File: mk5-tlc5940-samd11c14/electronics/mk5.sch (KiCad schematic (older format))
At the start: 49 parts, among them J1 Conn_01x08_Male, J10 Conn_01x01, J11 Conn_01x01, J12 Conn_01x01, J13 Conn_01x01, J14 Conn_01x01, J15 Conn_01x01, J16 Conn_01x01, J17 Conn_01x01, J18 Conn_01x01, J19 Conn_01x01, J2 USB, J20 Conn_01x01, J21 Conn_01x01, J22 Conn_01x01, J23 +LED, J24 +LED, J25 +LED, J26 +LED, J27 +LED, J3 OUT15, J4 GS2, J6 +LED, J7 Conn_01x01, J8 Conn_01x01, J9 Conn_01x01, Q1 MOSFET 20V 3A, SW1 BTN, U1 USBLC6-2SC6, U2 MCP1702-3302_SOT23, U3 SAMD11C14A, U4 TLC5940PWP

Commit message: Start refactoring for QFN24 version
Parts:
- removed J1: Conn_01x08_Male, SMD-pads:CONN_8_SMD_FLAT, symbol Conn_01x08_Male
- removed R3, R4: 680, Resistors_SMD:R_0603, symbol R
- removed U3: SAMD11C14A, Housings_SOIC:SOIC-14_3.9x8.7mm_Pitch1.27mm, symbol SAMD11C14A
- added J1: Conn_01x06_Male, SMD-pads:CONN_6_SMD_FLAT, symbol Conn_01x06_Male
- added U3: SAMD11D14A-M, Housings_DFN_QFN:QFN-24_4x4mm_Pitch0.5mm, symbol SAMD11D14A-M
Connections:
- net labels added: BLANK, BUTTON, Button, RESET, SCLK, SIN, SWCLK, SWDIO
- net labels removed: BLANK/RESET, SCK/SWCLK, SIN/SWDIO
- wire segments 133 -> 118
- no-connect marks 3 -> 11
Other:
- note added: "Do not use PA10, PA11, PA17, PA27 \nfor compatibility with SOIC-20"
- moved on the sheet: C3, C4, D3, J10, J11, J12, J13, J14, J15, J16, J17, J18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

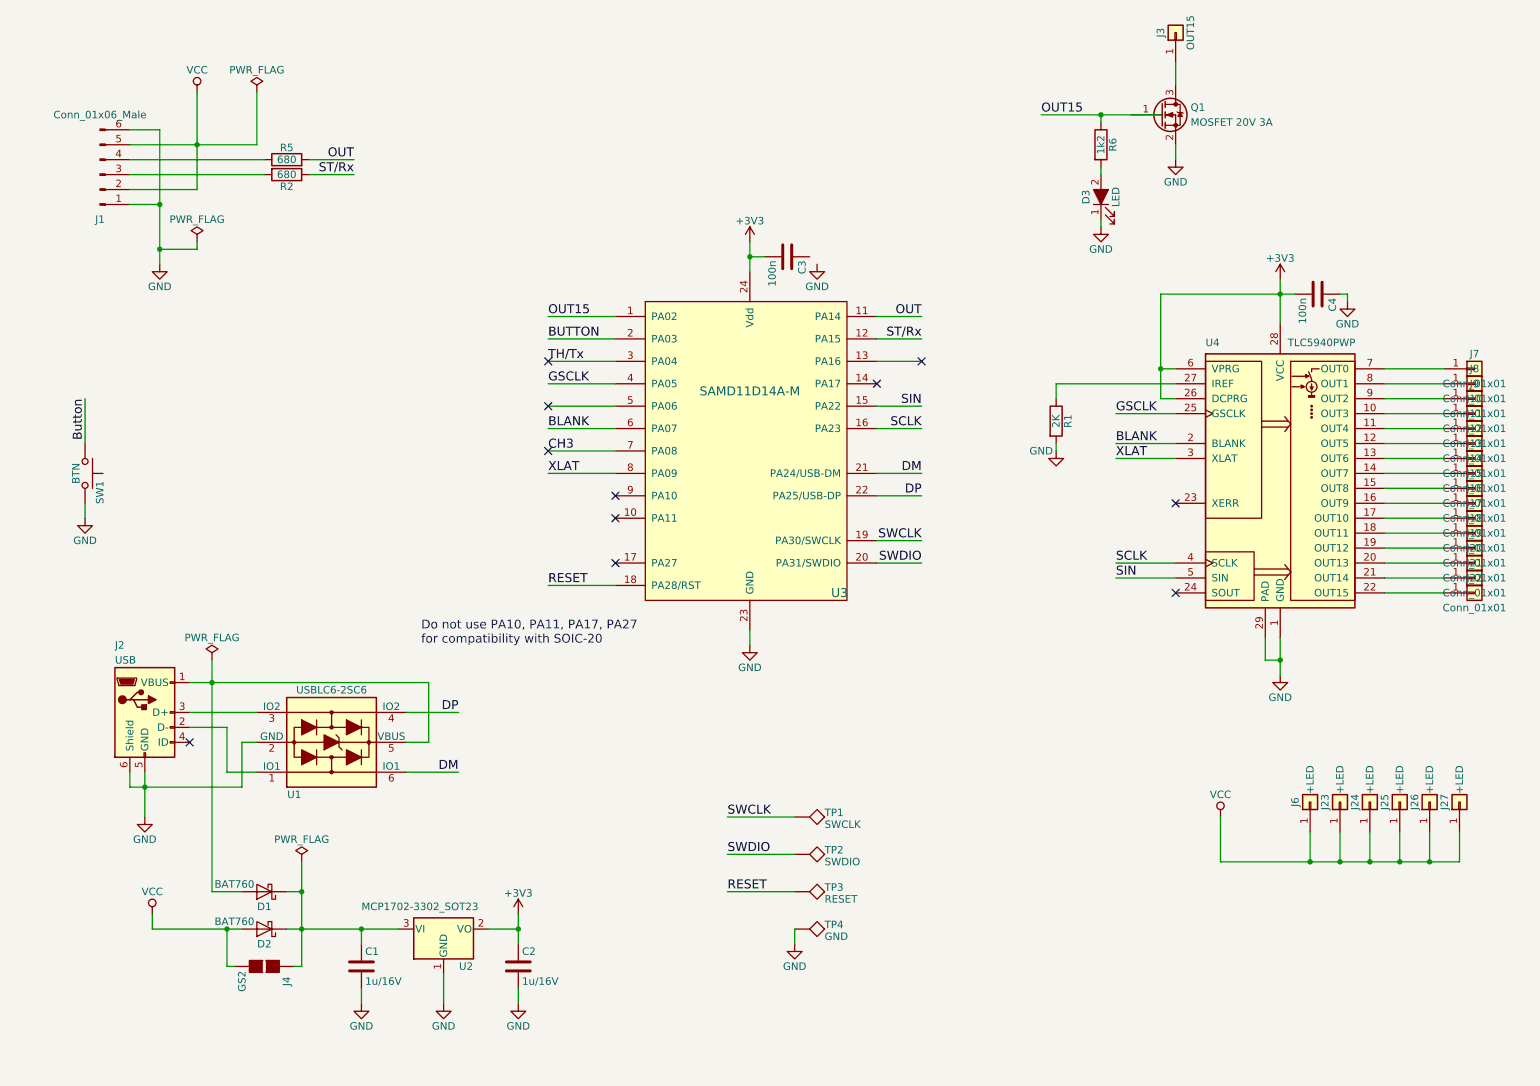
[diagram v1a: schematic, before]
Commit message: Try to figure out component placement for QFN version
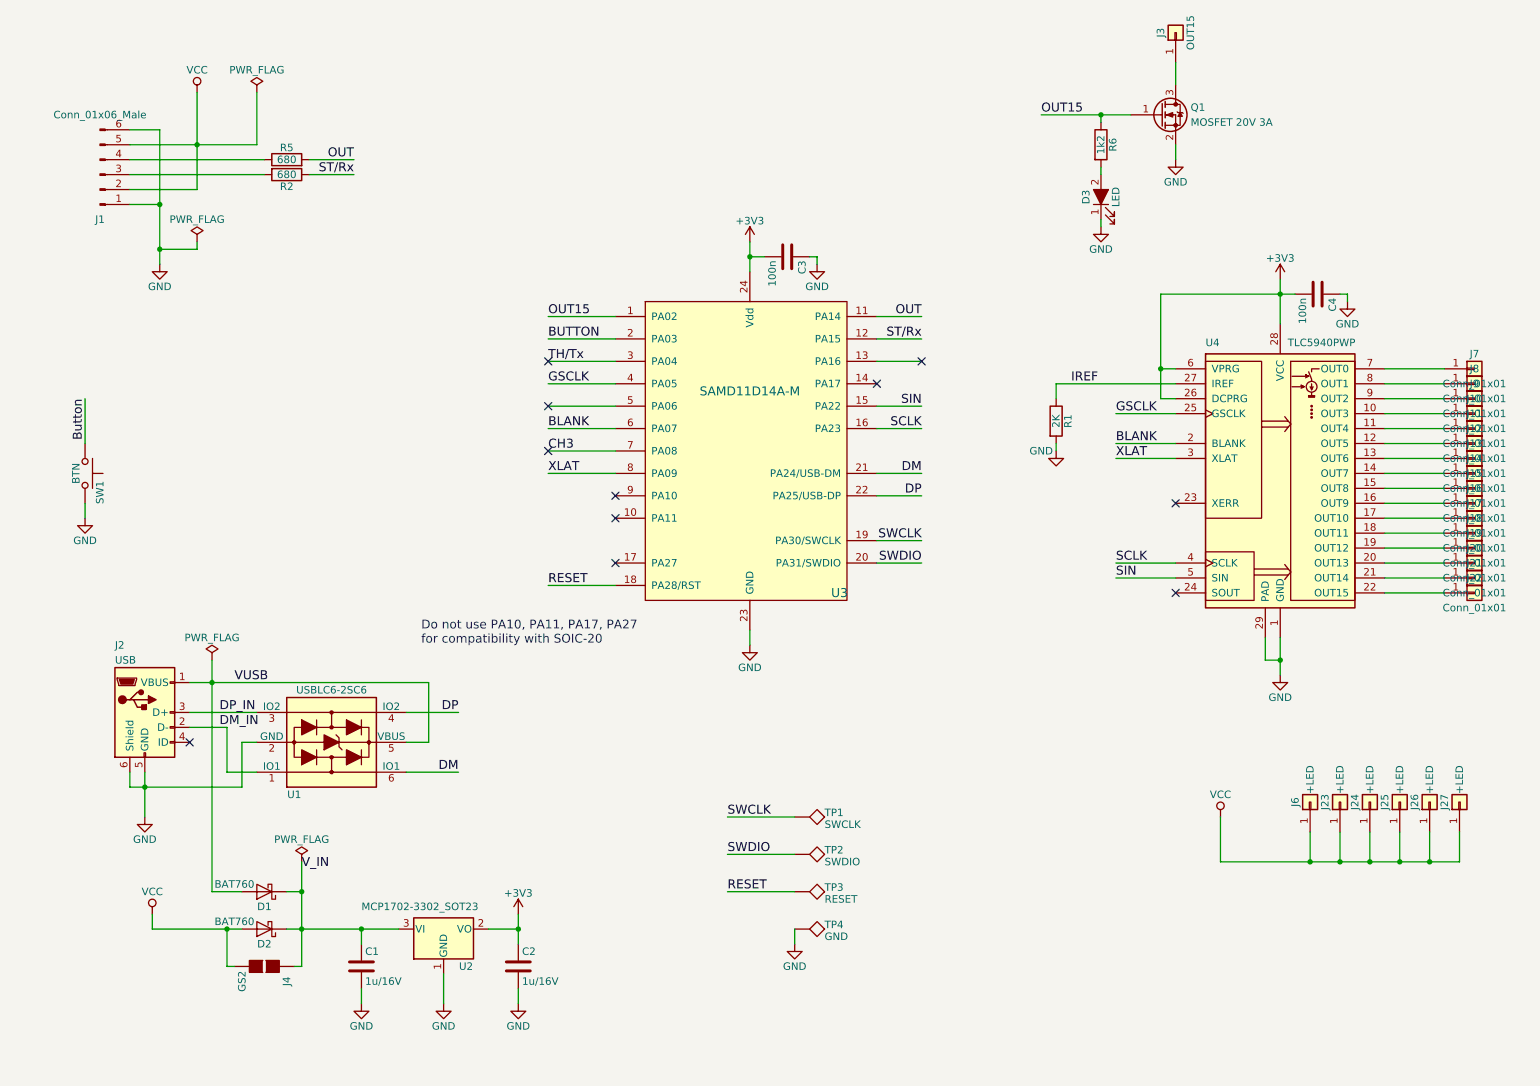
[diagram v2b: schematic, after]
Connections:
- net GND: now also C3.1
- net OUT15: now also Q1.1 (G)
- net IREF: now reaches R1.1, U4.27 (IREF)
- net VUSB: now reaches D1.2 (A), J2.1 (VBUS), U1.5 (VBUS)
- net DM_IN: now reaches J2.2 (D-), U1.1 (IO1)
- net DP_IN: now reaches J2.3 (D+), U1.3 (IO2)
- net V_IN: now reaches C1.1, D1.1 (K), D2.1 (K), J4.1 (G1), U2.3 (VI)
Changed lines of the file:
@@
 	4350 2600 4800 2600
 Wire Wire Line
-	7650 1250 8450 1250
+	7650 1250 8250 1250
 $Comp
 L R R2
@@
 Text Notes 3500 4800 0    59   ~ 0
 Do not use PA10, PA11, PA17, PA27 \nfor compatibility with SOIC-20
+Wire Wire Line
+	6100 2200 6150 2200
+Wire Wire Line
+	6150 2200 6150 2250
+Text Label 2250 5050 0    60   ~ 0
+VUSB
+Text Label 2150 5250 0    60   ~ 0
+DP_IN
+Text Label 2150 5350 0    60   ~ 0
+DM_IN
+Text Label 2700 6300 0    60   ~ 0
+V_IN
+Text Label 7850 3050 0    60   ~ 0
+IREF
 $EndSCHEMATC

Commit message: Change MCU pins for better layout
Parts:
- removed D1, D2: BAT760, Diodes_SMD:D_SOD-323_HandSoldering, symbol D_Schottky
- added D1: BAT54C, TO_SOT_Packages_SMD:SOT-23, symbol BAT54C
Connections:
- net BLANK: now also U3.7 (PA08); no longer U3.6 (PA07)
- net CH3: now also U3.16 (PA23); no longer U3.7 (PA08)
- net GSCLK: now also U3.13 (PA16); no longer U3.4 (PA05)
- net SCLK: now also U3.4 (PA05); no longer U3.16 (PA23)
- net SIN: now also U3.3 (PA04); no longer U3.15 (PA22)
- net TH/Tx: now also U3.15 (PA22); no longer U3.3 (PA04)
- net VCC: now also J4.1 (G1), D1.1; no longer J4.2 (G2)
- net VUSB: now also D1.2
- net V_IN: now also J4.2 (G2), D1.3; no longer J4.1 (G1)
- net XLAT: now also U3.6 (PA07); no longer U3.8 (PA09)
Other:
- moved on the sheet: J4
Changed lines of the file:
@@
 EESchema Schematic File Version 2
 LIBS:SAM_D11
+LIBS:bat54c
 LIBS:power
 LIBS:device
@@
 	1    0    0    -1
 $EndComp
-$Comp
-L D_Schottky D2
-U 1 1 59C47D22
-P 2450 6700
-F 0 "D2" H 2450 6800 50  0000 C CNN
-F 1 "BAT760" H 2650 6650 50  0000 C CNN
-F 2 "Diodes_SMD:D_SOD-323_HandSoldering" H 2450 6700 50  0001 C CNN
-F 3 "" H 2450 6700 50  0001 C CNN
-	1    2450 6700
-	-1   0    0    1
-$EndComp
-$Comp
-L D_Schottky D1
-U 1 1 59C47DAA
-P 2450 6450
-F 0 "D1" H 2450 6550 50  0000 C CNN
-F 1 "BAT760" H 2650 6400 50  0000 C CNN
-F 2 "Diodes_SMD:D_SOD-323_HandSoldering" H 2450 6450 50  0001 C CNN
-F 3 "" H 2450 6450 50  0001 C CNN
-	1    2450 6450
-	-1   0    0    1
-$EndComp
 Wire Wire Line
 	5700 4700 5700 4800
@@
 	3650 7000 3650 7200
 Wire Wire Line
-	2600 6700 3350 6700
-Wire Wire Line
 	3100 6700 3100 6800
 Wire Wire Line
@@
 	3100 7100 3100 7200
 Connection ~ 3100 6700
-Wire Wire Line
-	2600 6450 2700 6450
-Wire Wire Line
-	2700 6250 2700 6950
 Connection ~ 2700 6700
 Wire Wire Line
-	2100 4900 2100 6450
-Wire Wire Line
-	2100 6450 2300 6450
-Wire Wire Line
-	1700 6700 2300 6700
+	2100 4900 2100 6400
 $Comp
 L Conn_01x01 J3
@@
 L PWR_FLAG #FLG016
 U 1 1 59C4CC7B
-P 2700 6250
-F 0 "#FLG016" H 2700 6325 50  0001 C CNN
-F 1 "PWR_FLAG" H 2700 6400 50  0000 C CNN
-F 2 "" H 2700 6250 50  0001 C CNN
-F 3 "" H 2700 6250 50  0001 C CNN
-	1    2700 6250
-	1    0    0    -1
-$EndComp
-Connection ~ 2700 6450
+P 2700 6550
+F 0 "#FLG016" H 2700 6625 50  0001 C CNN
+F 1 "PWR_FLAG" H 2700 6700 50  0000 C CNN
+F 2 "" H 2700 6550 50  0001 C CNN
+F 3 "" H 2700 6550 50  0001 C CNN
+	1    2700 6550
+	1    0    0    -1
+$EndComp
 $Comp
 L GND #PWR017
@@
 L VCC #PWR019
 U 1 1 59C4E307
-P 1700 6600
-F 0 "#PWR019" H 1700 6450 50  0001 C CNN
-F 1 "VCC" H 1700 6750 50  0000 C CNN
-F 2 "" H 1700 6600 50  0001 C CNN
-F 3 "" H 1700 6600 50  0001 C CNN
-	1    1700 6600
-	1    0    0    -1
-$EndComp
-Wire Wire Line
-	1700 6600 1700 6700
+P 1700 6950
+F 0 "#PWR019" H 1700 6800 50  0001 C CNN
+F 1 "VCC" H 1700 7100 50  0000 C CNN
+F 2 "" H 1700 6950 50  0001 C CNN
+F 3 "" H 1700 6950 50  0001 C CNN
+	1    1700 6950
+	1    0    0    -1
+$EndComp
+Wire Wire Line
+	1700 6950 1700 7100
 Wire Wire Line
 	2000 1100 2000 1750
-Wire Wire Line
-	4350 2600 4800 2600
 Wire Wire Line
 	7650 1250 8250 1250
@@
 	2000 2150 1750 2150
 Connection ~ 1750 2150
-Text Label 4350 3650 0    60   ~ 0
+Text Label 4350 3350 0    60   ~ 0
 XLAT
 Text Label 4350 2600 0    60   ~ 0
@@
 L GS2 J4
 U 1 1 59DCA798
-P 2450 6950
-F 0 "J4" H 2550 7100 50  0000 C CNN
-F 1 "GS2" H 2550 6801 50  0000 C CNN
-F 2 "SMD-pads:SMD_solder_jumper_2pin" V 2524 6950 50  0001 C CNN
-F 3 "" H 2450 6950 50  0001 C CNN
-	1    2450 6950
-	0    1    1    0
-$EndComp
-Wire Wire Line
-	2700 6950 2650 6950
-Wire Wire Line
-	2250 6950 2200 6950
-Wire Wire Line
-	2200 6950 2200 6700
-Connection ~ 2200 6700
+P 2500 6900
+F 0 "J4" H 2600 7050 50  0000 C CNN
+F 1 "GS2" H 2600 6751 50  0000 C CNN
+F 2 "SMD-pads:SMD_solder_jumper_2pin" V 2574 6900 50  0001 C CNN
+F 3 "" H 2500 6900 50  0001 C CNN
+	1    2500 6900
+	-1   0    0    1
+$EndComp
 Wire Wire Line
 	9250 4750 9250 5000
@@
 NoConn ~ 6550 3050
 NoConn ~ 4800 4250
-Text Label 4350 3350 0    60   ~ 0
+Text Label 4350 3500 0    60   ~ 0
 BLANK
 Wire Wire Line
 	4800 2900 4350 2900
-Text Label 4350 2900 0    60   ~ 0
+Text Label 6850 3200 2    60   ~ 0
 TH/Tx
-Text Label 4350 3050 0    60   ~ 0
+Text Label 6850 2900 2    60   ~ 0
 GSCLK
 Wire Wire Line
@@
 Wire Wire Line
 	4800 3500 4350 3500
-Text Label 4350 3500 0    60   ~ 0
+Text Label 6850 3350 2    60   ~ 0
 CH3
 $Comp
@@
 	1    0    0    1
 $EndComp
-NoConn ~ 4350 3500
-NoConn ~ 4350 2900
 Wire Wire Line
 	6550 3350 6850 3350
-Text Label 6850 3350 2    60   ~ 0
+Text Label 4350 3050 0    60   ~ 0
 SCLK
-Text Label 6850 3200 2    60   ~ 0
+Text Label 4350 2900 0    60   ~ 0
 SIN
 Wire Wire Line
@@
 Wire Wire Line
 	6550 2900 6850 2900
-NoConn ~ 6850 2900
 Wire Wire Line
 	4800 3200 4350 3200
-NoConn ~ 4350 3200
 Text Notes 3500 4800 0    59   ~ 0
 Do not use PA10, PA11, PA17, PA27 \nfor compatibility with SOIC-20
@@
 Text Label 2150 5350 0    60   ~ 0
 DM_IN
-Text Label 2700 6300 0    60   ~ 0
+Text Label 2800 6700 0    60   ~ 0
 V_IN
 Text Label 7850 3050 0    60   ~ 0
 IREF
+Wire Wire Line
+	4800 2600 4350 2600
+NoConn ~ 6850 3200
+NoConn ~ 6850 3350
+NoConn ~ 4350 3200
+NoConn ~ 4350 3650
+$Comp
+L BAT54C D1
+U 1 1 5A105797
+P 2100 6700
+F 0 "D1" H 2125 6550 50  0000 L CNN
+F 1 "BAT54C" H 1850 6825 50  0000 L CNN
+F 2 "TO_SOT_Packages_SMD:SOT-23" H 2175 6825 50  0001 L CNN
+F 3 "" H 1970 6700 50  0001 C CNN
+	1    2100 6700
+	0    -1   -1   0
+$EndComp
+Wire Wire Line
+	1700 7100 2500 7100
+Wire Wire Line
+	2100 7100 2100 7000
+Connection ~ 2100 7100
+Wire Wire Line
+	2300 6700 3350 6700
+Connection ~ 2500 6700
+Wire Wire Line
+	2700 6550 2700 6700
 $EndSCHEMATC

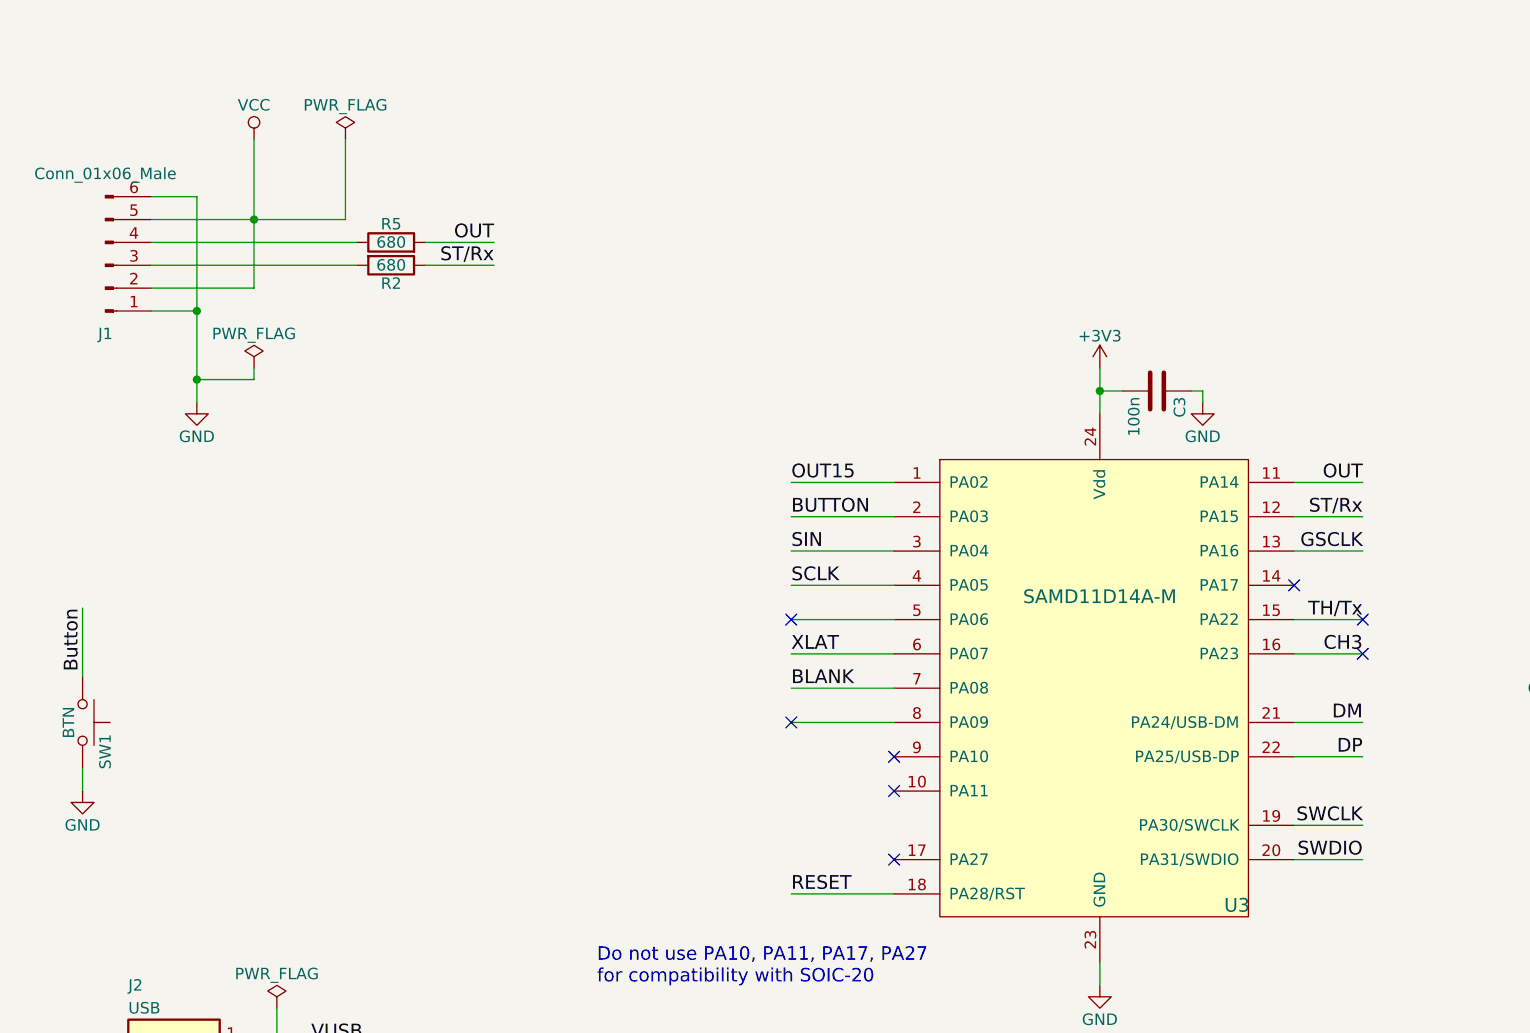
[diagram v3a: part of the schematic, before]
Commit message: Work on layout, remove push-button
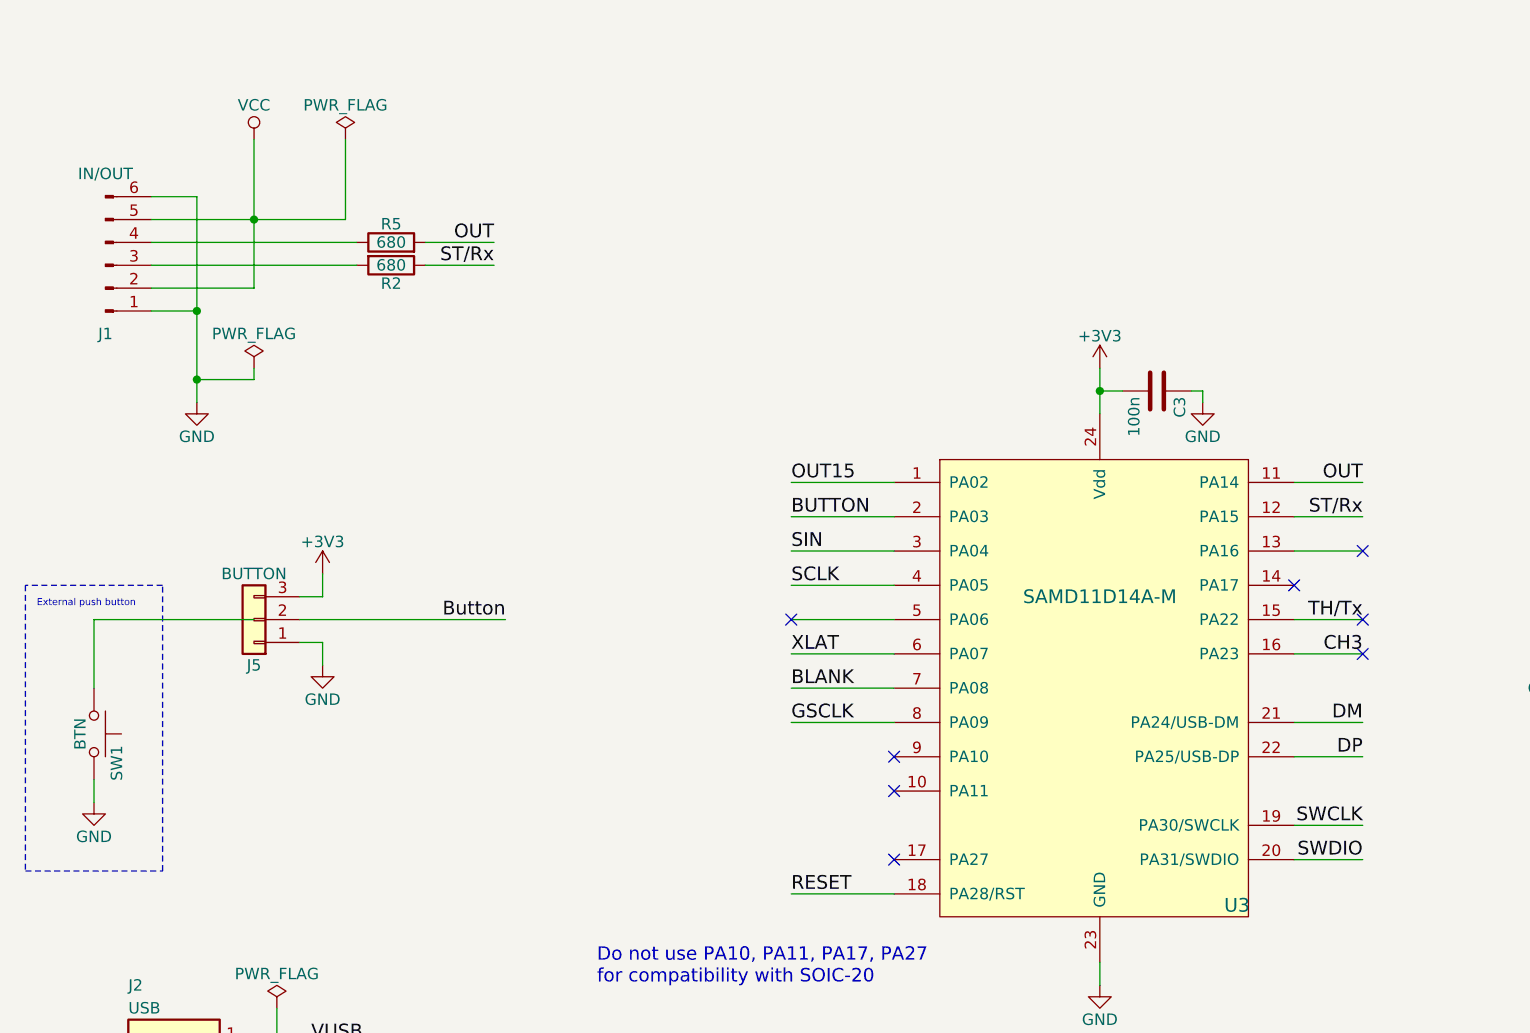
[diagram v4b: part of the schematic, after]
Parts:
- added J5: BUTTON, Socket_Strips:Socket_Strip_Straight_1x03, symbol Conn_01x03
- J1: value Conn_01x06_Male -> IN/OUT
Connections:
- net +3V3: now also J5.3 (Pin_3)
- net Button: now also J5.2 (Pin_2); no longer SW1.1
- net GND: now also J5.1 (Pin_1)
- net GSCLK: now also U3.8 (PA09); no longer U3.13 (PA16)
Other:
- note added: "External push button"
- moved on the sheet: SW1
